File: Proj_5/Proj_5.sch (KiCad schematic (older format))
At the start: 0 parts

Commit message: 11 errors left
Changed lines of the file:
@@
 F34 "A0" I L 3450 4600 50
 F35 "A1" I L 3450 4500 50
+F36 "~INTA" I R 8100 4400 50
+F37 "INT" O R 8100 4500 50
 $EndSheet
 $Sheet
@@
 F28 "D4" B R 28150 14100 50
 F29 "D3" B R 28150 14000 50
+F30 "R~W" I L 25850 13900 50
+F31 "RS" I L 25850 14000 50
 $EndSheet
 Entry Wire Line
@@
 Text Label 28350 14400 2    50   ~ 0
 D7
-Wire Bus Line
-	3400 7650 3400 7950
-Wire Bus Line
-	7750 11350 7750 13600
-Wire Bus Line
-	2450 1250 2450 7650
-Wire Bus Line
-	16950 9800 16950 10250
-Wire Bus Line
-	19150 11450 19150 15000
-Wire Bus Line
-	7200 9000 7200 9800
-Wire Bus Line
-	8700 1750 8700 3100
-Wire Bus Line
-	7500 11450 7500 13150
-Wire Bus Line
-	17000 4900 17000 6400
-Wire Bus Line
-	29100 1250 29100 10250
-Wire Bus Line
-	3100 2800 3100 6150
-Wire Bus Line
-	28450 2250 28450 14600
-Wire Bus Line
-	28000 2250 28000 4100
-Wire Bus Line
-	17000 6900 17000 8800
-Wire Bus Line
-	24550 2600 24550 4500
-Wire Bus Line
-	24450 4500 24450 13350
-Wire Bus Line
-	4250 11550 4250 14100
-Wire Bus Line
-	4000 6150 4000 11550
-Wire Bus Line
-	25350 13350 25350 17250
-Wire Bus Line
-	23550 13350 23550 16250
 Text Label 7650 13300 2    50   ~ 0
 ~RD
@@
 Text Label 28900 8700 2    50   ~ 0
 ~RD
+Wire Wire Line
+	23150 14000 23300 14000
+Wire Wire Line
+	23300 14000 23300 4200
+Wire Wire Line
+	23300 4200 14000 4200
+Wire Bus Line
+	3400 7650 3400 7950
+Wire Bus Line
+	7750 11350 7750 13600
+Wire Bus Line
+	2450 1250 2450 7650
+Wire Bus Line
+	16950 9800 16950 10250
+Wire Bus Line
+	19150 11450 19150 15000
+Wire Bus Line
+	7200 9000 7200 9800
+Wire Bus Line
+	8700 1750 8700 3100
+Wire Bus Line
+	7500 11450 7500 13150
+Wire Bus Line
+	17000 4900 17000 6400
+Wire Bus Line
+	29100 1250 29100 10250
+Wire Bus Line
+	3100 2800 3100 6150
+Wire Bus Line
+	28450 2250 28450 14600
+Wire Bus Line
+	28000 2250 28000 4100
+Wire Bus Line
+	17000 6900 17000 8800
+Wire Bus Line
+	24550 2600 24550 4500
+Wire Bus Line
+	24450 4500 24450 13350
+Wire Bus Line
+	4250 11550 4250 14100
+Wire Bus Line
+	4000 6150 4000 11550
+Wire Bus Line
+	25350 13350 25350 17250
+Wire Bus Line
+	23550 13350 23550 16250
 $EndSCHEMATC

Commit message: 1 Error Remains
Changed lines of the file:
@@
 F43 "RESET" I L 14100 5150 50
 F44 "NMI_IN" I L 14100 6350 50
+F45 "~INTA_OUT" O L 14100 6450 50
+F46 "INTR_IN" I L 14100 6550 50
 $EndSheet
 Text Label 19250 6150 0    118  ~ 0
@@
 ~WR
 Text Label 28900 4500 2    50   ~ 0
-~OE
+~RD
 Wire Wire Line
 	27450 4600 29000 4600
@@
 Wire Wire Line
 	23300 4200 14000 4200
+Wire Wire Line
+	8100 4400 13150 4400
+Wire Wire Line
+	13150 4400 13150 6450
+Wire Wire Line
+	13150 6450 14100 6450
+Wire Wire Line
+	8100 4500 13050 4500
+Wire Wire Line
+	13050 4500 13050 6550
+Wire Wire Line
+	13050 6550 14100 6550
 Wire Bus Line
 	3400 7650 3400 7950

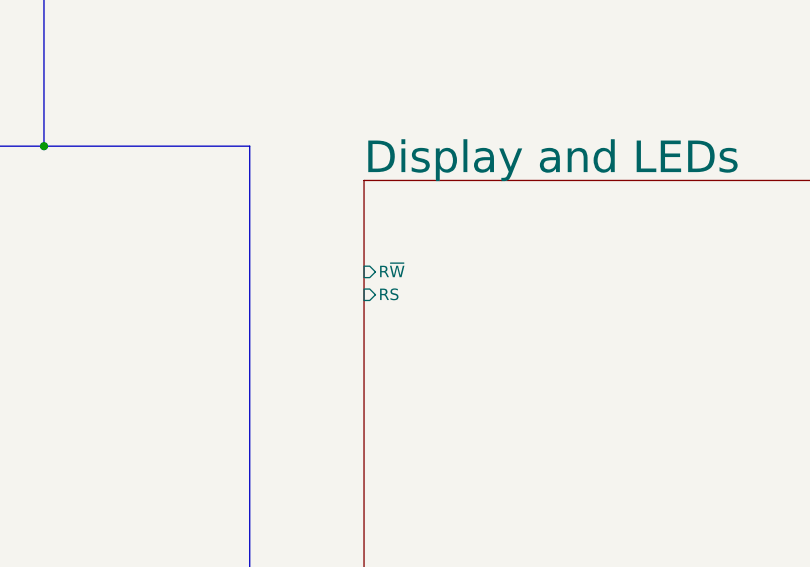
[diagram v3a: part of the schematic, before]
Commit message: Added 5 Footprints
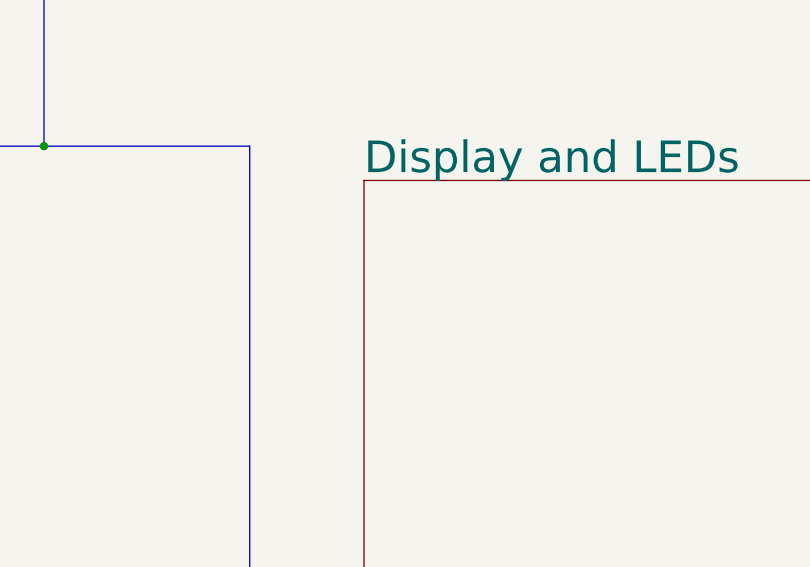
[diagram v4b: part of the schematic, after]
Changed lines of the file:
@@
 F28 "D4" B R 28150 14100 50
 F29 "D3" B R 28150 14000 50
-F30 "R~W" I L 25850 13900 50
-F31 "RS" I L 25850 14000 50
 $EndSheet
 Entry Wire Line

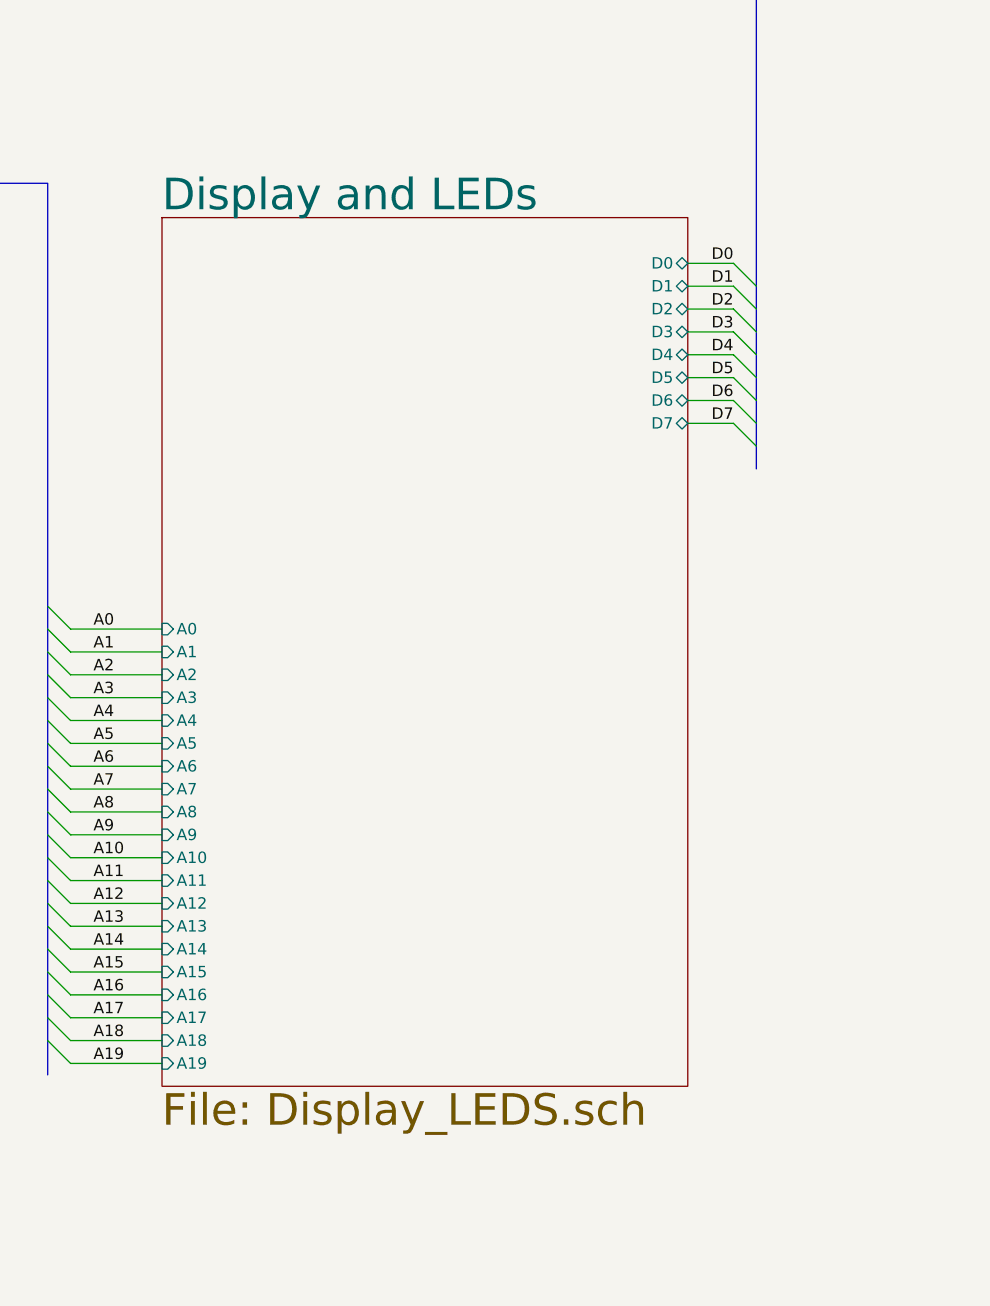
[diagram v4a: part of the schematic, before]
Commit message: Added at least 4 Footprints
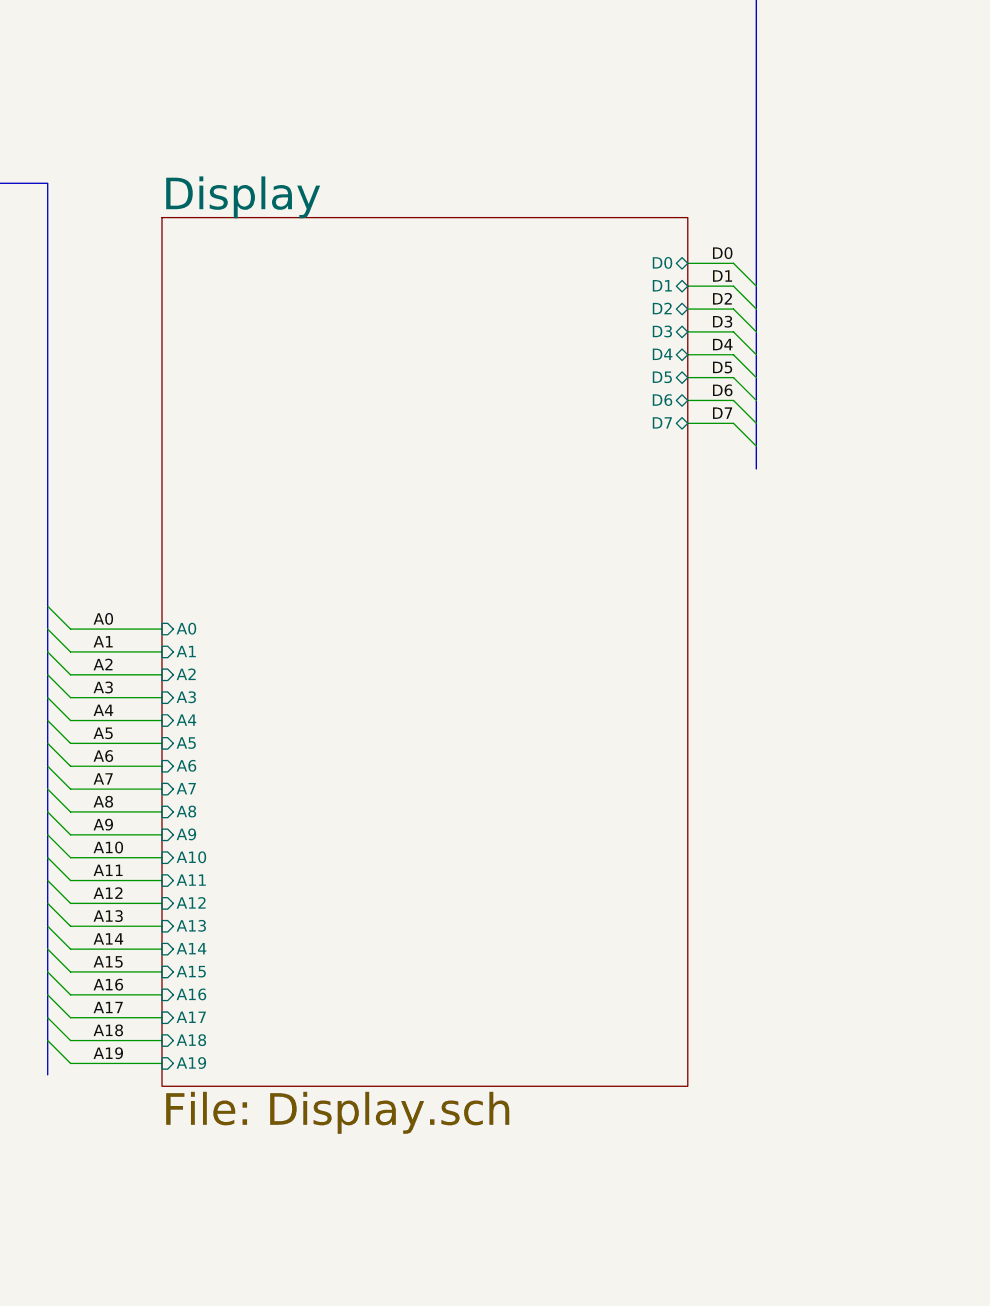
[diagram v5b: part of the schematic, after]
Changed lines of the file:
@@
 S 25850 13500 2300 3800
 U 5EAF7226
-F0 "Display and LEDs" 138
-F1 "Display_LEDS.sch" 138
+F0 "Display" 138
+F1 "Display.sch" 138
 F2 "A12" I L 25850 16500 50
 F3 "A15" I L 25850 16800 50

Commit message: Data Aquired
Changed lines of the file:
@@
 F4 "RES_OUT" O L 14800 2950 50
-$EndSheet
-$Sheet
-S 24850 7300 2600 2600
-U 5EA98353
-F0 "SRAM Memory" 256
-F1 "CY7C199.sch" 256
-F2 "A12" I L 24850 8600 50
-F3 "A15" I L 24850 8900 50
-F4 "A16" I L 24850 9000 50
-F5 "A11" I L 24850 8500 50
-F6 "A13" I L 24850 8700 50
-F7 "A14" I L 24850 8800 50
-F8 "A19" I L 24850 9300 50
-F9 "A18" I L 24850 9200 50
-F10 "A17" I L 24850 9100 50
-F11 "D3" B R 27450 7750 50
-F12 "D4" B R 27450 7850 50
-F13 "D5" B R 27450 7950 50
-F14 "D6" B R 27450 8050 50
-F15 "D7" B R 27450 8150 50
-F16 "D2" B R 27450 7650 50
-F17 "D1" B R 27450 7550 50
-F18 "D0" B R 27450 7450 50
-F19 "A0" I L 24850 7400 50
-F20 "A10" I L 24850 8400 50
-F21 "A9" I L 24850 8300 50
-F22 "A8" I L 24850 8200 50
-F23 "A7" I L 24850 8100 50
-F24 "A6" I L 24850 8000 50
-F25 "A5" I L 24850 7900 50
-F26 "A4" I L 24850 7800 50
-F27 "A3" I L 24850 7700 50
-F28 "A2" I L 24850 7600 50
-F29 "A1" I L 24850 7500 50
-F30 "~OE" I R 27450 8700 50
-F31 "~WE" I R 27450 8600 50
-F32 "~BHE" I R 27450 8800 50
-F33 "M~IO" I R 27450 8900 50
 $EndSheet
 Text Notes 28400 22050 0    169  ~ 0
@@
 Wire Wire Line
 	13050 6550 14100 6550
+Entry Wire Line
+	28450 9150 28350 9050
+Entry Wire Line
+	28450 9250 28350 9150
+Entry Wire Line
+	28450 9350 28350 9250
+Entry Wire Line
+	28450 9450 28350 9350
+Entry Wire Line
+	28450 9550 28350 9450
+Entry Wire Line
+	28450 9650 28350 9550
+Entry Wire Line
+	28450 9750 28350 9650
+Entry Wire Line
+	28450 9850 28350 9750
+Wire Wire Line
+	27450 9050 28350 9050
+Wire Wire Line
+	27450 9150 28350 9150
+Wire Wire Line
+	27450 9250 28350 9250
+Wire Wire Line
+	27450 9350 28350 9350
+Wire Wire Line
+	27450 9450 28350 9450
+Wire Wire Line
+	27450 9550 28350 9550
+Wire Wire Line
+	27450 9650 28350 9650
+Wire Wire Line
+	27450 9750 28350 9750
+$Sheet
+S 24850 7300 2600 2600
+U 5EA98353
+F0 "SRAM Memory" 256
+F1 "CY7C199.sch" 256
+F2 "A12" I L 24850 8600 50
+F3 "A15" I L 24850 8900 50
+F4 "A16" I L 24850 9000 50
+F5 "A11" I L 24850 8500 50
+F6 "A13" I L 24850 8700 50
+F7 "A14" I L 24850 8800 50
+F8 "A19" I L 24850 9300 50
+F9 "A18" I L 24850 9200 50
+F10 "A17" I L 24850 9100 50
+F11 "D3" B R 27450 7750 50
+F12 "D4" B R 27450 7850 50
+F13 "D5" B R 27450 7950 50
+F14 "D6" B R 27450 8050 50
+F15 "D7" B R 27450 8150 50
+F16 "D2" B R 27450 7650 50
+F17 "D1" B R 27450 7550 50
+F18 "D0" B R 27450 7450 50
+F19 "A0" I L 24850 7400 50
+F20 "A10" I L 24850 8400 50
+F21 "A9" I L 24850 8300 50
+F22 "A8" I L 24850 8200 50
+F23 "A7" I L 24850 8100 50
+F24 "A6" I L 24850 8000 50
+F25 "A5" I L 24850 7900 50
+F26 "A4" I L 24850 7800 50
+F27 "A3" I L 24850 7700 50
+F28 "A2" I L 24850 7600 50
+F29 "A1" I L 24850 7500 50
+F30 "~OE" I R 27450 8700 50
+F31 "~WE" I R 27450 8600 50
+F32 "~BHE" I R 27450 8800 50
+F33 "M~IO" I R 27450 8900 50
+F34 "D8" B R 27450 9050 50
+F35 "D9" B R 27450 9150 50
+F36 "D10" B R 27450 9250 50
+F37 "D11" B R 27450 9350 50
+F38 "D12" B R 27450 9450 50
+F39 "D13" B R 27450 9550 50
+F40 "D15" B R 27450 9750 50
+F41 "D14" B R 27450 9650 50
+$EndSheet
+Text Label 28200 9750 0    50   ~ 0
+D15
+Text Label 28200 9650 0    50   ~ 0
+D14
+Text Label 28200 9550 0    50   ~ 0
+D13
+Text Label 28200 9450 0    50   ~ 0
+D12
+Text Label 28200 9350 0    50   ~ 0
+D11
+Text Label 28200 9250 0    50   ~ 0
+D10
+Text Label 28250 9150 0    50   ~ 0
+D9
+Text Label 28250 9050 0    50   ~ 0
+D8
 Wire Bus Line
 	3400 7650 3400 7950
@@
 	3100 2800 3100 6150
 Wire Bus Line
+	28000 2250 28000 4100
+Wire Bus Line
+	17000 6900 17000 8800
+Wire Bus Line
+	24550 2600 24550 4500
+Wire Bus Line
+	24450 4500 24450 13350
+Wire Bus Line
+	4250 11550 4250 14100
+Wire Bus Line
+	4000 6150 4000 11550
+Wire Bus Line
 	28450 2250 28450 14600
 Wire Bus Line
-	28000 2250 28000 4100
-Wire Bus Line
-	17000 6900 17000 8800
-Wire Bus Line
-	24550 2600 24550 4500
-Wire Bus Line
-	24450 4500 24450 13350
-Wire Bus Line
-	4250 11550 4250 14100
-Wire Bus Line
-	4000 6150 4000 11550
-Wire Bus Line
 	25350 13350 25350 17250

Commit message: Wires are Hell
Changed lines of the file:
@@
 	14800 2950 13650 2950
 Wire Wire Line
-	13650 2950 13650 5150
+	13650 2950 13650 3500
 Wire Wire Line
 	13650 5150 14100 5150
-Wire Wire Line
-	13650 5150 13650 11250
 Connection ~ 13650 5150
 Wire Wire Line
@@
 Connection ~ 4250 11550
 Wire Wire Line
-	13650 11250 3600 11250
-Wire Wire Line
-	3600 11250 3600 7850
-Wire Wire Line
 	3600 7850 4400 7850
-Connection ~ 13650 11250
-Wire Wire Line
-	13650 11250 13650 13950
 $Sheet
 S 25850 13500 2300 3800
@@
 Text Label 28250 9050 0    50   ~ 0
 D8
+Wire Wire Line
+	13650 5150 13650 13950
+Wire Wire Line
+	3600 7850 3600 6750
+Wire Wire Line
+	3600 6750 12250 6750
+Wire Wire Line
+	12250 6750 12250 3500
+Wire Wire Line
+	12250 3500 13650 3500
 Wire Bus Line
 	3400 7650 3400 7950
@@
 Wire Bus Line
 	23550 13350 23550 16250
+Connection ~ 13650 3500
+Wire Wire Line
+	13650 3500 13650 5150
 $EndSCHEMATC
